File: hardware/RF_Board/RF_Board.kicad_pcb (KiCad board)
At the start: 4 copper layers, 90 x 90 mm, 129 parts, among them J1 Conn_Coaxial, J2 Conn_01x07_Male, J3 Conn_Coaxial, J4 Conn_01x07_Male, J5 Conn_01x06_Female, J6 Conn_01x06_Female, J7 Conn_01x06_Female, J8 L77TSAH15SOL2RM8, Q1 2N7002, Q2 2N7002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

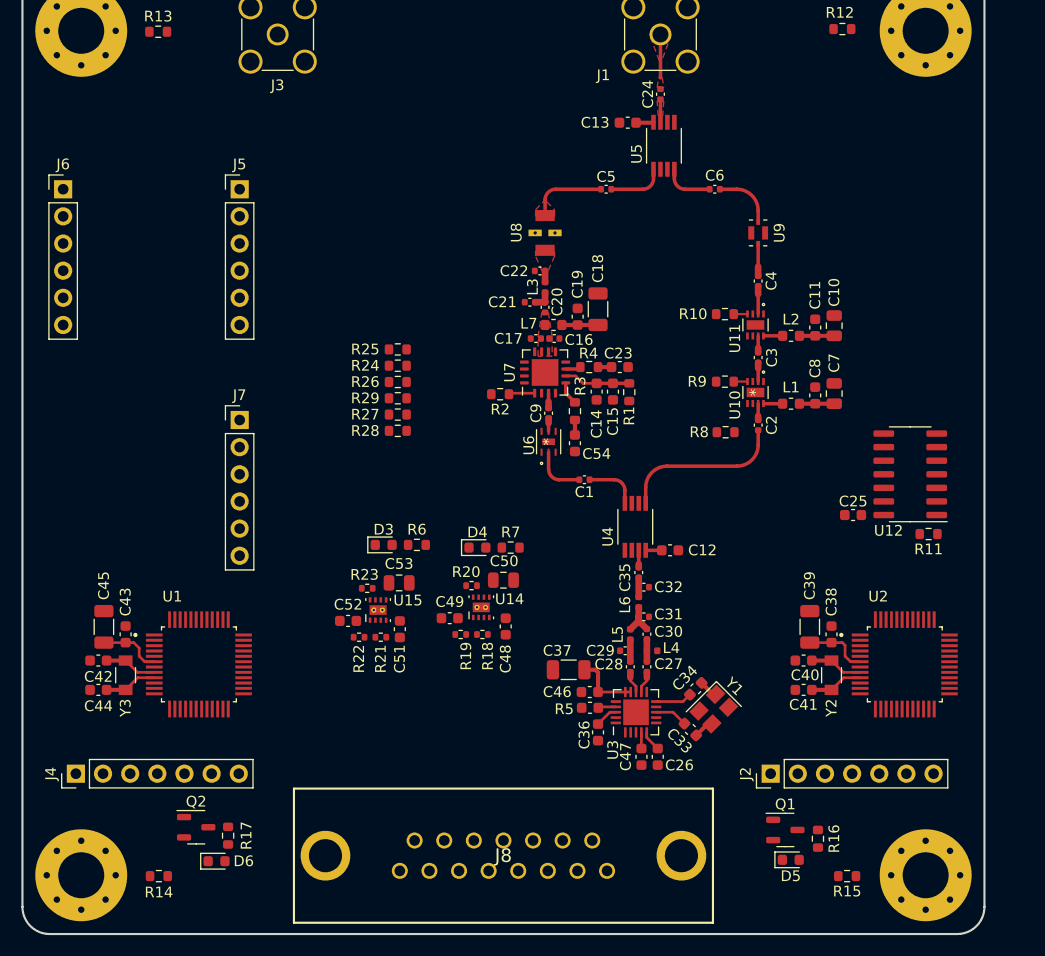
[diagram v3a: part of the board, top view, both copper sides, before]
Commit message: add UHF module to RF board
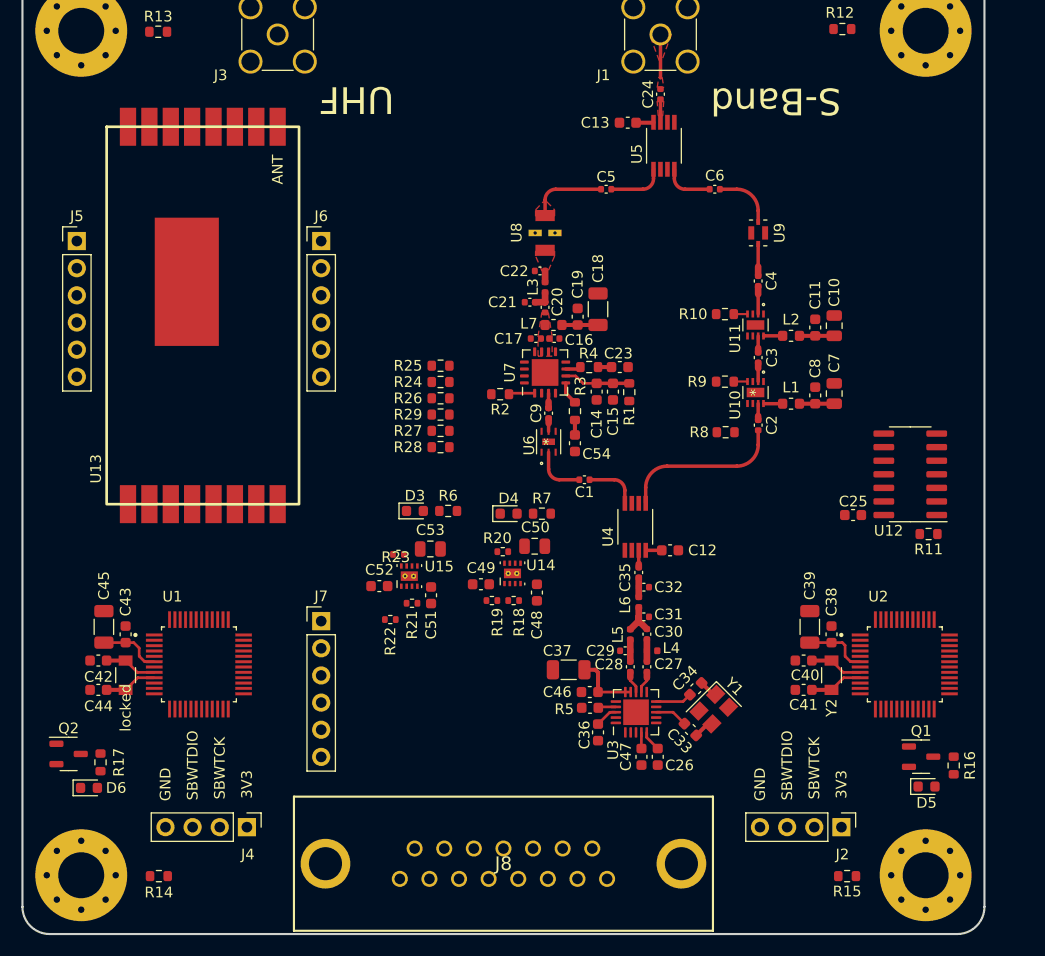
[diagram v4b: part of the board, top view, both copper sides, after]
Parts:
- added U13: RFM95PW, RF_Board_Footprints:RFM95PW, F.Cu at (23.9, 14.5)
- J2, J4: value Conn_01x07_Male -> Conn_01x04_Male; footprint RF_Board_Footprints:PinHeader_1x07_P2.54mm_Vertical -> RF_Board_Footprints:PinHeader_1x04_P2.54mm_Vertical
- moved J6 24.6 mm to (27.9, 25.2)
- moved J7 20.3 mm to (27.9, 60.7)
- moved J4 16.8 mm to (21.0, 80.0), turned to -90 degrees
- moved J5 16.0 mm to (5.09, 25.2)
- moved R16 14.4 mm to (87.1, 74.2)
- moved Q1 14.4 mm to (84.1, 73.4)
- moved D5 14.4 mm to (84.6, 76.2)
- moved D6 13.8 mm to (6.22, 76.3)
- moved Q2 13.8 mm to (4.32, 73.2)
- moved R17 13.8 mm to (7.30, 73.9)
- moved J2 8.30 mm to (76.6, 80.0), turned to -90 degrees
- moved C52 4.37 mm to (33.4, 57.5)
- moved C50 4.31 mm to (47.9, 53.7)
- moved C51 4.31 mm to (38.2, 58.3)
- moved D3 4.31 mm to (36.7, 50.4)
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- renumbered Y3 to locked
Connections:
- J2 pad 1: /CC2500_SBWTCK -> +3.3V
- J2 pad 2: /CC2500_SBWTDIO -> /CC2500_SBWTCK
- J2 pad 3: /CC2500_UART_TX_2 -> /CC2500_SBWTDIO
- J2 pad 4: /CC2500_UART_RX_2 -> GND
- J4 pad 1: /RFM_SBWTCK -> +3.3V
- J4 pad 2: /RFM_SBWTDIO -> /RFM_SBWTCK
- J4 pad 3: /RFM_UART_TX_2 -> /RFM_SBWTDIO
- J4 pad 4: /RFM_UART_RX_2 -> GND
- J6 pad 1: /RFM_DIO5 -> /RFM_DIO3
- J6 pad 2: /RFM_DIO2 -> /RFM_DIO4
- J6 pad 3: /RFM_DIO1 -> /RFM_DIO0
- J6 pad 4: /RFM_DIO0 -> /RFM_DIO1
- J6 pad 5: /RFM_DIO4 -> /RFM_DIO2
- J6 pad 6: /RFM_DIO3 -> /RFM_DIO5
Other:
- board text added: "3V3"
- board text added: "GND"
- board text added: "S-Band"
- board text added: "SBWTCK"
- board text added: "SBWTDIO"
- board text added: "UHF"

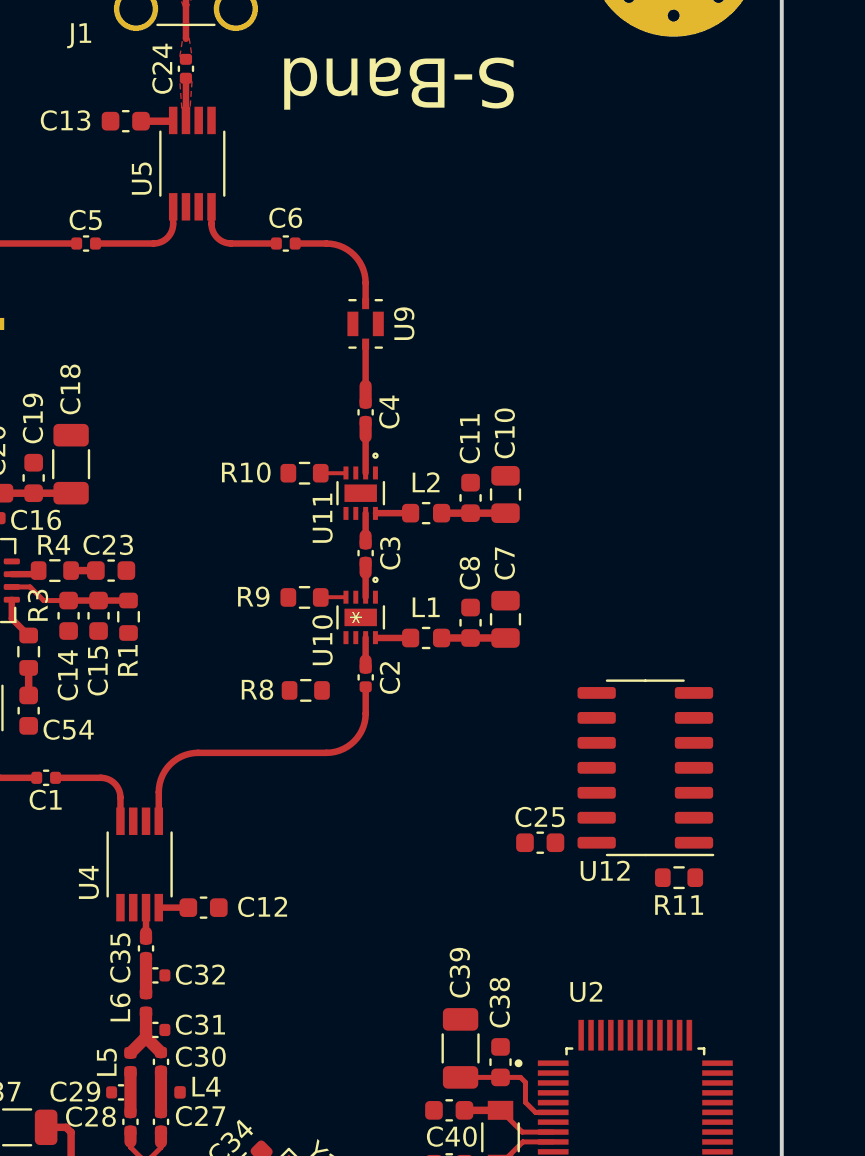
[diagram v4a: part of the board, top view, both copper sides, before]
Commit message: start RF board digital routing
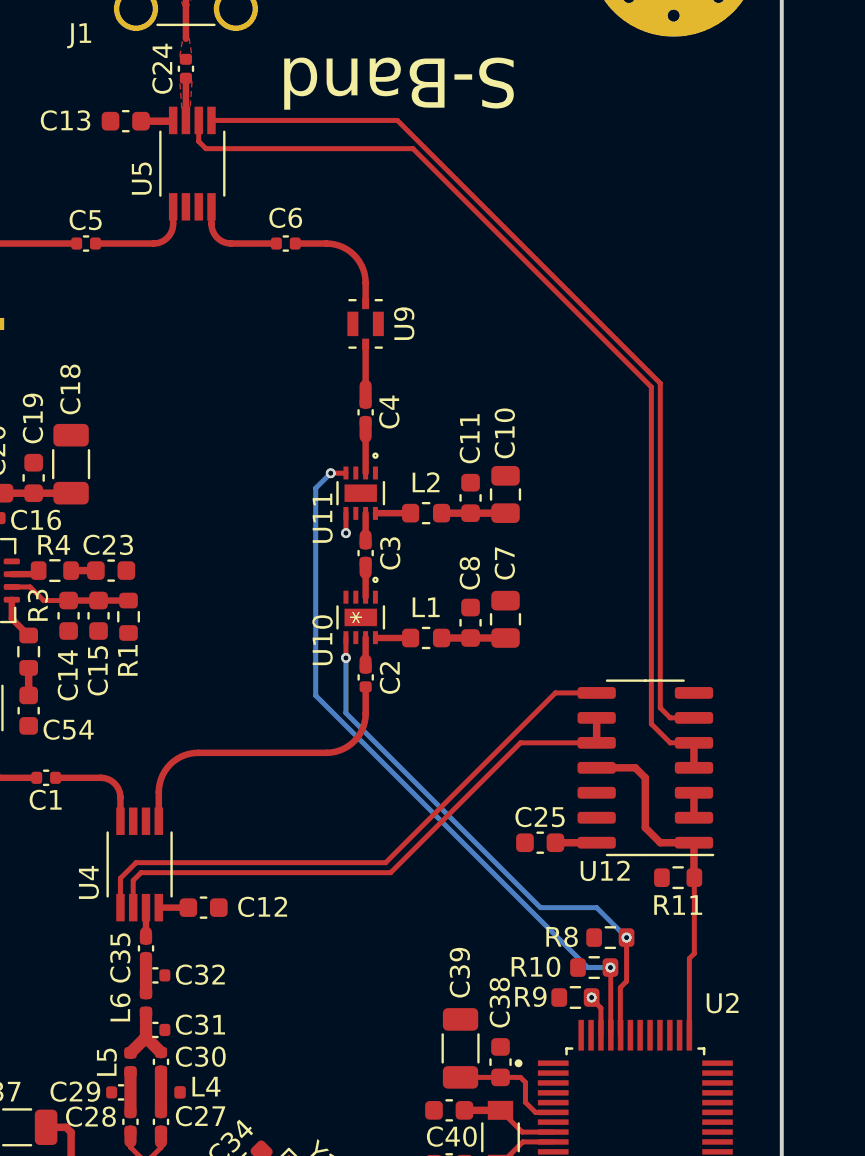
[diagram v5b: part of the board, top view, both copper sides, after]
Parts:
- moved R10 29.1 mm to (80.5, 57.1)
- moved R9 24.6 mm to (79.5, 58.7)
- moved R8 20.0 mm to (81.3, 55.6)
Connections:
- J7 pad 1: unconnected-(J7-Pad1) -> GND
- J7 pad 2: unconnected-(J7-Pad2) -> GND
- J7 pad 5: GND -> unconnected-(J7-Pad5)
- J7 pad 6: GND -> unconnected-(J7-Pad6)
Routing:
- net /SW2_B: track 0.00 -> 50.2 mm
- net /SW2_A: track 0.00 -> 46.8 mm
- net /LNA_BP_B: track 1.29 -> 36.6 mm, vias 0 -> 2
- net /SW1_A: track 0.00 -> 29.6 mm
- net /SW1_B: track 0.00 -> 29.1 mm
- net /LNA_SD: track 0.00 -> 28.9 mm, vias 0 -> 3
- net /SBAND_TX_RX: track 0.00 -> 17.9 mm
- net +3.3V: track 21.8 -> 23.9 mm
- net Net-(U12-Pad2): track 0.00 -> 1.27 mm
- net /LNA_BP_A: track 1.29 -> 2.11 mm, vias 0 -> 1
